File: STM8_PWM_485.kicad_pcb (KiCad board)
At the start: 2 copper layers, 22 x 28 mm, 30 parts, among them P1 SWIM, P2 PWR, P3 PWM_1, P4 PWM_485, P5 485_EN, U1 nRF24L01_12x18mm, U2 STM8S103K3, U3 MC78M05CDT, U4 AMS1117, U5 MAX487

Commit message: PCB
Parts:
- moved R8 79.2 mm to (117.8, 95.2), turned to 180 degrees
- moved C4 77.0 mm to (107.1, 102.5), turned to 90 degrees
- moved R6 76.2 mm to (115.2, 95.2)
- moved R9 75.8 mm to (113.5, 102.5), turned to 90 degrees
- moved R10 74.8 mm to (120.4, 95.2)
- moved C1 74.5 mm to (114.8, 97.8), turned to 90 degrees
- moved C2 74.1 mm to (105.1, 108.7), turned to 270 degrees
- moved R7 72.5 mm to (115.0, 102.5), turned to 270 degrees
- moved R3 69.8 mm to (109.9, 102.2), turned to 270 degrees
- moved R2 69.4 mm to (106.0, 115.3)
- moved R5 69.3 mm to (111.8, 102.2), turned to 90 degrees
- moved C3 69.1 mm to (105.1, 112.3), turned to 90 degrees
- moved R1 64.8 mm to (108.6, 102.5), turned to 270 degrees
- moved C9 60.8 mm to (117.6, 112.5), turned to 90 degrees
- moved C8 59.4 mm to (112.9, 115.4), turned to 180 degrees
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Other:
- board size 22 x 28 mm -> 22 x 38 mm

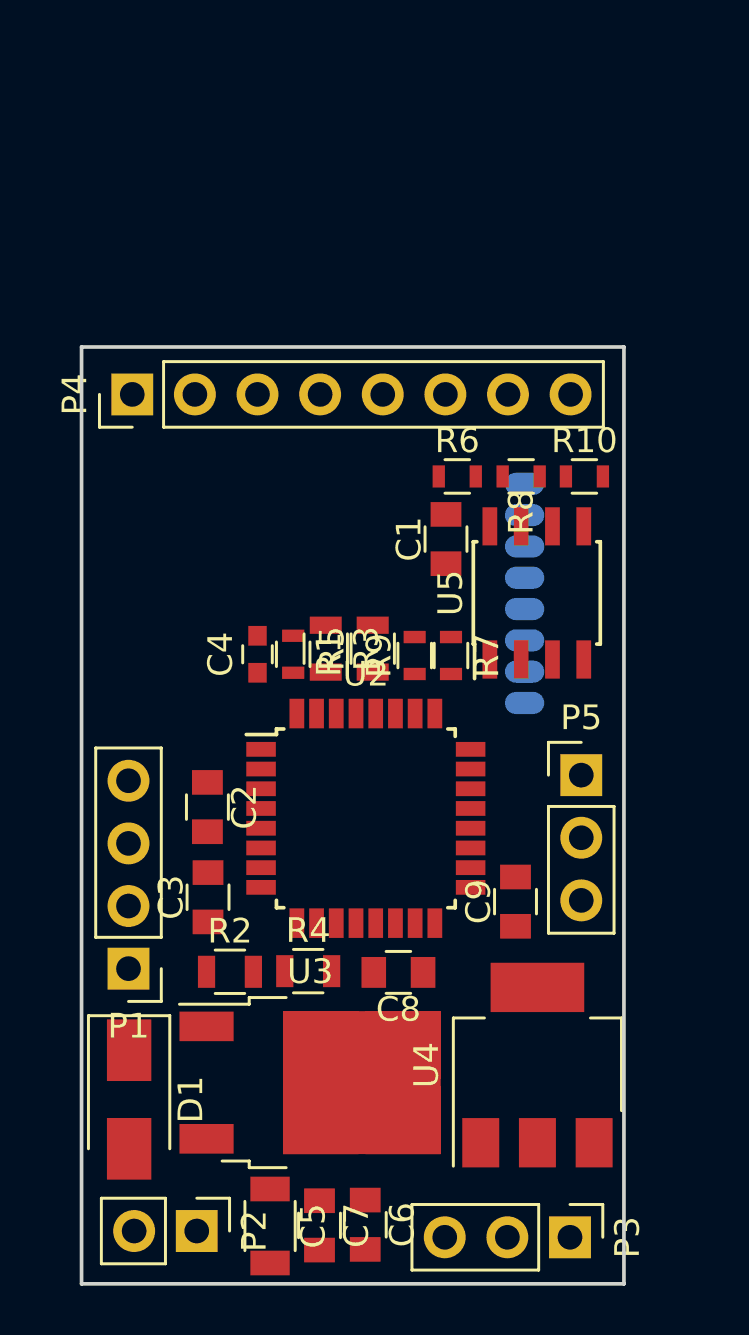
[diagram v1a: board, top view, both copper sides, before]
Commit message: hange to STM32
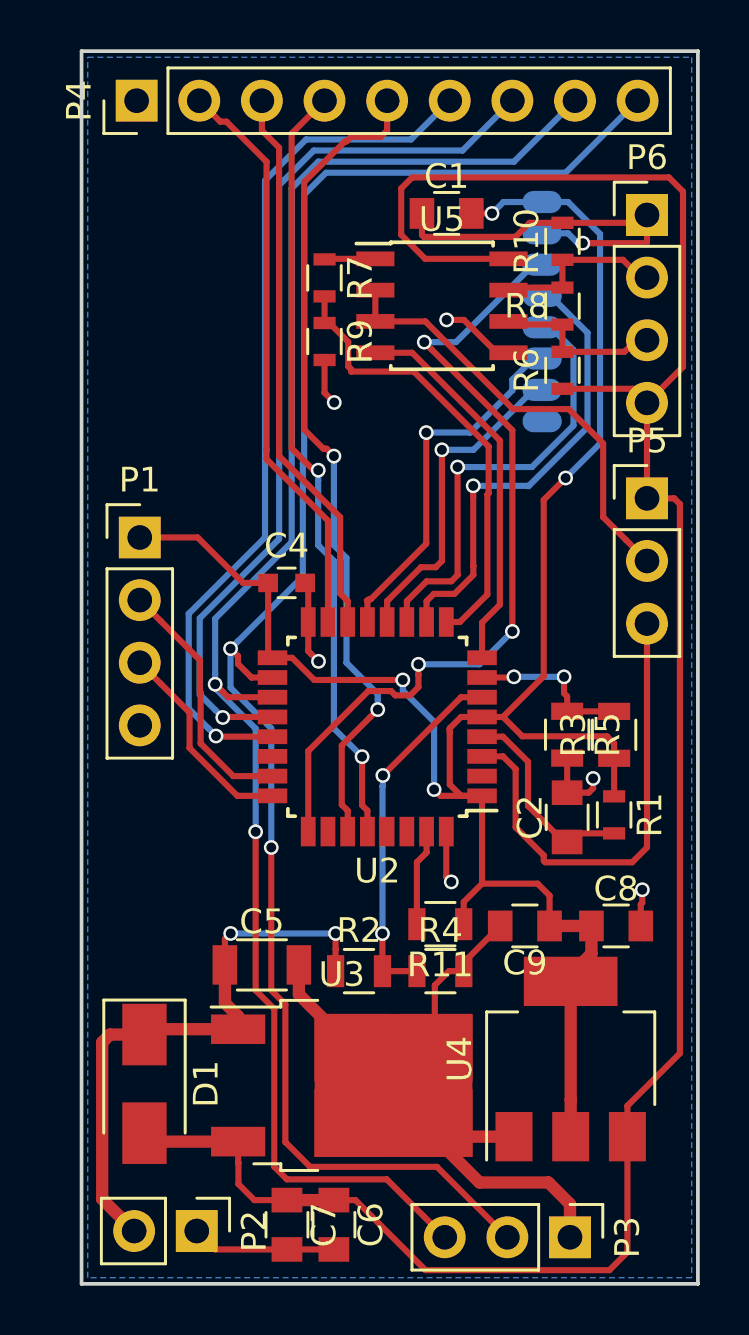
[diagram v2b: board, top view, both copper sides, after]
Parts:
- removed C3: 1u, Capacitors_SMD:C_0805
- added P6: 485, Pin_Headers:Pin_Header_Straight_1x04_Pitch2.54mm, F.Cu at (122.9, 84.6)
- added R11: 10K, Resistors_SMD:R_0805, F.Cu at (114.6, 113.4)
- P1: value SWIM -> SWD
- P4: value PWM_485 -> PWM; footprint Pin_Headers:Pin_Header_Straight_1x08_Pitch2.54mm -> Pin_Headers:Pin_Header_Straight_1x09_Pitch2.54mm
- U2: value STM8S103K3 -> STM32F030K6
- moved P1 17.5 mm to (102.4, 97.7), turned to 0 degrees
- moved R7 16.2 mm to (109.9, 87.2)
- moved C2 14.6 mm to (119.7, 109.1), turned to 90 degrees
- moved R1 14.6 mm to (121.6, 109.0)
- moved R9 13.3 mm to (109.9, 89.8), turned to 270 degrees
- moved C1 13.2 mm to (114.8, 84.6), turned to 0 degrees
- moved U5 12.3 mm to (114.6, 88.3), turned to 0 degrees
- moved R3 12.2 mm to (121.6, 105.7), turned to 90 degrees
- moved P4 11.9 mm to (102.2, 80.0)
- moved P5 11.5 mm to (122.9, 96.1)
- moved U1 11.5 mm to (110.0, 88.5)
- moved C5 10.6 mm to (107.3, 115.1), turned to 0 degrees
- moved R10 9.58 mm to (119.5, 85.7), turned to 90 degrees
- moved C8 9.03 mm to (121.7, 113.5), turned to 0 degrees
- moved R5 8.62 mm to (119.7, 105.7), turned to 270 degrees
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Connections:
- C2 pad 1: GND -> /NRST
- C2 pad 2: +3V3 -> GND
- C4 pad 1: /NRST -> +3V3
- P1 pad 2: /SWIM -> /SWDIO
- P1 pad 3: GND -> /SWCLK
- P1 pad 4: /NRST -> GND
- P4 pad 2: /PWM_6 -> /PWM_8
- P4 pad 3: /PWM_5 -> /PWM_7
- P4 pad 4: /PWM_4 -> /PWM_6
- P4 pad 5: /PWM_3 -> /PWM_5
- P4 pad 6: /485_B -> /PWM_4
- P4 pad 7: /485_A -> /PWM_3
- P4 pad 8: GND -> /PWM_2
- U1 pad 8: /IRQ -> Net-(U1-Pad8)
- U2 pad 1: /NRST -> +3V3
- U2 pad 10: (no net) -> /CSN
- U2 pad 11: (no net) -> /SCLK
- U2 pad 12: (no net) -> /MISO
- U2 pad 13: (no net) -> /MOSI
- U2 pad 14: (no net) -> /PWM_7
- U2 pad 15: /AD1 -> /PWM_8
- U2 pad 16: /AD0 -> GND
- U2 pad 17: /CSN -> +3V3
- U2 pad 2: (no net) -> /Button1
- U2 pad 22: /SCLK -> /IRQ
- U2 pad 23: /MOSI -> /SWDIO
- U2 pad 24: /MISO -> /SWCLK
- U2 pad 26: /SWIM -> /LED
- U2 pad 27: /IRQ -> /PWM_5
- U2 pad 29: /PWM_5 -> /SCL
- U2 pad 3: (no net) -> /DE
- U2 pad 30: /TxD -> /SDA
- U2 pad 31: /RxD -> /BOOT0
- U2 pad 32: /DE -> GND
- U2 pad 4: GND -> /NRST
- U2 pad 5: Net-(C3-Pad2) -> +3V3
- U2 pad 6: +3V3 -> /AD0
- U2 pad 7: (no net) -> /AD1
- U2 pad 8: (no net) -> /TxD
- U2 pad 9: (no net) -> /RxD
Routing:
- net +5V: track 0.00 -> 91.7 mm
- net +3V3: track 0.00 -> 82.9 mm, vias 0 -> 4
- net /PWM_1: track 0.00 -> 68.7 mm, vias 0 -> 2
- net /PWM_2: track 0.00 -> 65.6 mm, vias 0 -> 2
- net GND: track 0.00 -> 59.8 mm, vias 0 -> 7
- net /PWM_3: track 0.00 -> 36.2 mm, vias 0 -> 1
- net /PWM_4: track 0.00 -> 35.4 mm, vias 0 -> 1
- net /PWM_5: track 0.00 -> 33.8 mm, vias 0 -> 2
- net /CE: track 0.00 -> 33.5 mm, vias 0 -> 3
- net /PWM_6: track 0.00 -> 31.6 mm, vias 0 -> 2
- net +12V: track 0.00 -> 24.1 mm, vias 0 -> 2
- net /PWM_8: track 0.00 -> 23.5 mm
- net /PWM_7: track 0.00 -> 22.6 mm
- net /DE: track 0.00 -> 19.3 mm
- net /CSN: track 0.00 -> 18.7 mm, vias 0 -> 1
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- added copper zone on B.Cu, net GND
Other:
- board size 22 x 38 mm -> 25 x 50 mm

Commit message: PCB UPdate
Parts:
- added D2: ACT, LEDs:LED_0805, F.Cu at (119.6, 102.1)
- added R12: 1K, Resistors_SMD:R_0805, F.Cu at (119.7, 98.4)
- added R13: 10K, Resistors_SMD:R_0805, F.Cu at (102.1, 113.5)
- added REF***: KiCad-Logo_6mm_SilkScreen, Symbols:KiCad-Logo_6mm_SilkScreen, B.Cu at (113.4, 114.2)
- added REF***: OSHW-Logo_11.4x12mm_SilkScreen, Symbols:OSHW-Logo_11.4x12mm_SilkScreen, B.Cu at (113.3, 103.2)
- added SW1: SW, Pin_Headers:Pin_Header_Straight_1x02_Pitch2.00mm, F.Cu at (102.4, 108.9)
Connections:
- U2 pad 2: /Button1 -> /SW1
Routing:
- net /SW1: track 0.00 -> 20.5 mm, vias 0 -> 2
- net +3V3: track 82.9 -> 103.1 mm, vias 4 -> 6
- net /LED: track 0.00 -> 15.4 mm, vias 0 -> 2
- net +5V: track 91.7 -> 78.9 mm
- net GND: track 59.8 -> 55.6 mm, vias 7 -> 9
- net Net-(D2-Pad1): track 0.00 -> 1.65 mm
- net /DE: track 19.3 -> 20.6 mm
- net /PWM_5: track 33.8 -> 34.9 mm
- net /CE: track 33.5 -> 32.7 mm
- net /AD1: track 6.69 -> 6.36 mm, vias 2 -> 0
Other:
- board text added: "+"
- board text added: "-"
- board text added: "1"
- board text added: "2"
- board text added: "3.3V"
- board text added: "485 On Off"
- board text added: "5V"
- board text added: "8ch - 4 group CWW Led 2.4Ghz/RS485"
- board text added: "A"
- board text added: "B"
- board text added: "CLK"
- board text added: "G"
- board text added: "IO"
- board text added: "PWM"
- board text added: "PWM OUTPUTS"
- board text added: "PWR 24V Max"
- board text added: "SWD"
- board text added: "V1.0 BK 2017"

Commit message: PCB Update
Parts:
- removed the REF*** at (113.4, 114.2)
- removed the REF*** at (113.3, 103.2)
- added C3: 10u, Capacitors_SMD:C_0805, F.Cu at (112.3, 84.7)
- added REF***: KiCad-Logo2_8mm_SilkScreen, Symbols:KiCad-Logo2_8mm_SilkScreen, B.Cu at (112.7, 116.9)
- added REF***: OSHW-Logo_7.5x8mm_SilkScreen, Symbols:OSHW-Logo_7.5x8mm_SilkScreen, B.Cu at (108.4, 108.1)
- C4: footprint Capacitors_SMD:C_0603 -> Capacitors_SMD:C_0805
- R1, R7: value 10k -> 10K
- R11, R13, R4: footprint Resistors_SMD:R_0805 -> Resistors_SMD:R_0603
- moved C1 1.02 mm to (115.8, 84.7)
- moved R11 0.83 mm to (114.9, 114.2)
- moved R4 0.45 mm to (114.9, 115.6)
- moved C4 0.18 mm to (108.1, 99.6)
- moved R12 0.08 mm to (119.6, 98.4)
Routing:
- net GND: track 55.6 -> 62.1 mm
- net +3V3: track 103.1 -> 108.8 mm
- net /BOOT0: track 3.92 -> 4.57 mm
- net /AD0: track 14.9 -> 15.6 mm
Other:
- board text added: "485/2.4Ghz 8 channel 4 group CWW PWM Controller"
- board text added: "8"

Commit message: Update
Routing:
- net GND: track 62.1 -> 60.3 mm
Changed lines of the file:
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@@
   (general
     (links 97)
-    (no_connects 2)
+    (no_connects 0)
     (area 99.924999 77.924999 125.075001 128.075001)
     (thickness 1.6)
     (drawings 28)
-    (tracks 513)
+    (tracks 515)
     (zones 0)
     (modules 38)
@@
     (effects (font (size 1 1) (thickness 0.15)) (justify mirror))
   )
-  (gr_text G (at 102.235 81.8515 360) (layer B.SilkS)
+  (gr_text G (at 102.235 81.8515) (layer B.SilkS)
     (effects (font (size 1 1) (thickness 0.15)) (justify mirror))
   )
@@
   (segment (start 120.5725 108.077) (end 120.75 107.8995) (width 0.25) (layer F.Cu) (net 1))
   (segment (start 114.795 109.6555) (end 114.795 109.9555) (width 0.25) (layer F.Cu) (net 1))
-  (segment (start 120.1315 85.7885) (end 120.3325 85.7885) (width 0.25) (layer B.Cu) (net 1))
-  (segment (start 118.682 85.389) (end 119.732 85.389) (width 0.25) (layer B.Cu) (net 1))
-  (segment (start 119.732 85.389) (end 120.1315 85.7885) (width 0.25) (layer B.Cu) (net 1))
   (segment (start 109.195 101.1555) (end 109.195 99.694) (width 0.25) (layer F.Cu) (net 1))
   (segment (start 109.195 99.694) (end 109.069 99.568) (width 0.25) (layer F.Cu) (net 1))
@@
   (segment (start 105.4194 126.603) (end 104.6736 125.8572) (width 0.25) (layer F.Cu) (net 1))
   (segment (start 110.236 126.603) (end 108.331 126.603) (width 0.25) (layer F.Cu) (net 1))
+  (segment (start 120.8278 97.7392) (end 121.031 97.536) (width 0.25) (layer B.Cu) (net 2))
+  (segment (start 121.031 97.536) (end 121.031 89.0905) (width 0.25) (layer B.Cu) (net 2))
+  (segment (start 121.031 89.0905) (end 119.8245 87.884) (width 0.25) (layer B.Cu) (net 2))
+  (segment (start 119.8245 87.884) (end 119.8245 84.2115) (width 0.25) (layer B.Cu) (net 2))
+  (segment (start 119.8245 84.2115) (end 119.732 84.119) (width 0.25) (layer B.Cu) (net 2))
+  (segment (start 119.732 84.119) (end 118.682 84.119) (width 0.25) (layer B.Cu) (net 2))
   (segment (start 113.268 84.709) (end 113.268 83.834) (width 0.25) (layer F.Cu) (net 2))
   (segment (start 113.268 83.834) (end 113.409 83.693) (width 0.25) (layer F.Cu) (net 2))
@@
   (segment (start 120.8278 102.489) (end 121.7168 103.378) (width 0.25) (layer F.Cu) (net 2))
   (segment (start 120.8278 97.7392) (end 120.8278 102.489) (width 0.25) (layer F.Cu) (net 2))
-  (segment (start 121.031 97.536) (end 120.8278 97.7392) (width 0.25) (layer B.Cu) (net 2))
   (via (at 120.8278 97.7392) (size 0.6) (drill 0.4) (layers F.Cu B.Cu) (net 2))
-  (segment (start 121.031 93.9165) (end 121.031 97.536) (width 0.25) (layer B.Cu) (net 2))
   (segment (start 114.726621 105.235915) (end 115.02662 105.535914) (width 0.25) (layer B.Cu) (net 2))
   (segment (start 114.2238 104.733094) (end 114.726621 105.235915) (width 0.25) (layer B.Cu) (net 2))
@@
   (segment (start 121.6025 106.08) (end 121.3135 105.791) (width 0.25) (layer F.Cu) (net 2))
   (segment (start 117.095 105.0055) (end 116.245 105.0055) (width 0.25) (layer F.Cu) (net 2))
-  (segment (start 121.031 85.418) (end 121.031 93.9165) (width 0.25) (layer B.Cu) (net 2))
-  (segment (start 118.682 84.119) (end 119.732 84.119) (width 0.25) (layer B.Cu) (net 2))
-  (segment (start 119.732 84.119) (end 121.031 85.418) (width 0.25) (layer B.Cu) (net 2))
   (segment (start 114.935 105.4655) (end 114.935 105.664) (width 0.25) (layer F.Cu) (net 2))
   (segment (start 116.245 105.0055) (end 115.395 105.0055) (width 0.25) (layer F.Cu) (net 2))
@@
   (segment (start 108.206 124.603) (end 108.19 124.587) (width 0.5) (layer F.Cu) (net 5))
   (segment (start 110.236 124.603) (end 108.331 124.603) (width 0.5) (layer F.Cu) (net 5))
+  (segment (start 108.975998 94.695998) (end 108.975998 98.1075) (width 0.25) (layer B.Cu) (net 6))
+  (segment (start 106.045 101.038498) (end 108.975998 98.1075) (width 0.25) (layer B.Cu) (net 6))
+  (segment (start 106.045 102.235) (end 106.045 101.038498) (width 0.25) (layer B.Cu) (net 6))
   (segment (start 107.696 116.092587) (end 107.696 111.252) (width 0.25) (layer F.Cu) (net 6))
   (via (at 107.696 111.252) (size 0.6) (drill 0.4) (layers F.Cu B.Cu) (net 6))
@@
   (segment (start 106.045 103.8225) (end 107.696 105.4735) (width 0.25) (layer B.Cu) (net 6))
   (segment (start 106.045 102.235) (end 106.045 103.8225) (width 0.25) (layer B.Cu) (net 6))
-  (segment (start 108.975998 99.304002) (end 106.344999 101.935001) (width 0.25) (layer B.Cu) (net 6))
   (segment (start 109.0295 94.642496) (end 108.975998 94.695998) (width 0.25) (layer B.Cu) (net 6))
   (segment (start 109.0295 83.82) (end 109.0295 94.642496) (width 0.25) (layer B.Cu) (net 6))
   (segment (start 119.634 82.931) (end 109.9185 82.931) (width 0.25) (layer B.Cu) (net 6))
-  (segment (start 108.975998 94.695998) (end 108.975998 99.304002) (width 0.25) (layer B.Cu) (net 6))
   (segment (start 109.9185 82.931) (end 109.0295 83.82) (width 0.25) (layer B.Cu) (net 6))
   (segment (start 122.555 80.01) (end 119.634 82.931) (width 0.25) (layer B.Cu) (net 6))
-  (segment (start 106.344999 101.935001) (end 106.045 102.235) (width 0.25) (layer B.Cu) (net 6))
   (segment (start 106.045 102.235) (end 106.344999 102.534999) (width 0.25) (layer F.Cu) (net 6))
   (segment (start 106.344999 102.534999) (end 106.344999 102.855499) (width 0.25) (layer F.Cu) (net 6))
@@
   (segment (start 109.6051 82.480989) (end 108.5215 83.564589) (width 0.25) (layer B.Cu) (net 7))
   (segment (start 117.544011 82.480989) (end 109.6051 82.480989) (width 0.25) (layer B.Cu) (net 7))
+  (segment (start 111.8235 103.9495) (end 111.593063 104.179937) (width 0.25) (layer B.Cu) (net 8))
+  (segment (start 111.593063 104.179937) (end 111.593063 105.11064) (width 0.25) (layer B.Cu) (net 8))
+  (segment (start 111.8235 101.346) (end 111.8235 103.9495) (width 0.25) (layer B.Cu) (net 8))
+  (segment (start 110.236 99.7585) (end 111.8235 101.346) (width 0.25) (layer B.Cu) (net 8))
+  (segment (start 110.236 98.806) (end 110.236 99.7585) (width 0.25) (layer B.Cu) (net 8))
+  (segment (start 109.601 98.171) (end 110.236 98.806) (width 0.25) (layer B.Cu) (net 8))
+  (segment (start 109.601 95.420264) (end 109.601 98.171) (width 0.25) (layer B.Cu) (net 8))
   (segment (start 111.595 105.112577) (end 111.593063 105.11064) (width 0.25) (layer F.Cu) (net 8))
   (segment (start 111.595 109.6555) (end 111.595 105.112577) (width 0.25) (layer F.Cu) (net 8))
-  (segment (start 109.595491 95.425773) (end 109.595491 103.113068) (width 0.25) (layer B.Cu) (net 8))
   (segment (start 109.601 94.996) (end 109.601 95.420264) (width 0.25) (layer B.Cu) (net 8))
   (segment (start 109.601 95.420264) (end 109.595491 95.425773) (width 0.25) (layer B.Cu) (net 8))
-  (segment (start 109.595491 103.113068) (end 111.293064 104.810641) (width 0.25) (layer B.Cu) (net 8))
   (via (at 111.593063 105.11064) (size 0.6) (drill 0.4) (layers F.Cu B.Cu) (net 8))
-  (segment (start 111.293064 104.810641) (end 111.593063 105.11064) (width 0.25) (layer B.Cu) (net 8))
   (segment (start 109.601 94.996) (end 109.4105 94.996) (width 0.25) (layer F.Cu) (net 8))
   (via (at 109.601 94.996) (size 0.6) (drill 0.4) (layers F.Cu B.Cu) (net 8))
